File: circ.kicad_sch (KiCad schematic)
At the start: 2 parts

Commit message: Add files via upload
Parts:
- renumbered R22 to R30, U13 to U14
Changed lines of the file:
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@@
   (symbol (lib_id "Parts:J100N50X4B") (at 203.2 154.94 0) (unit 1)
     (in_bom yes) (on_board yes) (dnp no) (fields_autoplaced)
-    (property "Reference" "R22" (at 207.645 154.94 0)
+    (property "Reference" "R30" (at 207.645 154.94 0)
       (effects (font (size 1.27 1.27)) (justify left))
     )
@@
       (project "m17-rru-rf"
         (path "/4c42207c-9e6b-42da-ad38-da126b892014/52ad0992-68c2-4318-a1ac-e7f0506bc4fb"
-          (reference "R22") (unit 1)
+          (reference "R30") (unit 1)
         )
       )
@@
   (symbol (lib_id "Parts:WH3538X-1") (at 203.2 127 0) (unit 1)
     (in_bom yes) (on_board yes) (dnp no) (fields_autoplaced)
-    (property "Reference" "U13" (at 203.0795 115.4879 0)
+    (property "Reference" "U14" (at 203.0795 115.4879 0)
       (effects (font (size 1.27 1.27)))
     )
@@
       (project "m17-rru-rf"
         (path "/4c42207c-9e6b-42da-ad38-da126b892014/52ad0992-68c2-4318-a1ac-e7f0506bc4fb"
-          (reference "U13") (unit 1)
+          (reference "U14") (unit 1)
         )
       )

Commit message: Add files via upload
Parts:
- renumbered R30 to R34
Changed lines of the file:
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@@
   (symbol (lib_id "Parts:J100N50X4B") (at 203.2 154.94 0) (unit 1)
     (in_bom yes) (on_board yes) (dnp no) (fields_autoplaced)
-    (property "Reference" "R30" (at 207.645 154.94 0)
+    (property "Reference" "R34" (at 207.645 154.94 0)
       (effects (font (size 1.27 1.27)) (justify left))
     )
@@
       (project "m17-rru-rf"
         (path "/4c42207c-9e6b-42da-ad38-da126b892014/52ad0992-68c2-4318-a1ac-e7f0506bc4fb"
-          (reference "R30") (unit 1)
+          (reference "R34") (unit 1)
         )
       )

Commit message: Add files via upload
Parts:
- renumbered R34 to R37
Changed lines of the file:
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@@
   (symbol (lib_id "Parts:J100N50X4B") (at 203.2 154.94 0) (unit 1)
     (in_bom yes) (on_board yes) (dnp no) (fields_autoplaced)
-    (property "Reference" "R34" (at 207.645 154.94 0)
+    (property "Reference" "R37" (at 207.645 154.94 0)
       (effects (font (size 1.27 1.27)) (justify left))
     )
@@
       (project "m17-rru-rf"
         (path "/4c42207c-9e6b-42da-ad38-da126b892014/52ad0992-68c2-4318-a1ac-e7f0506bc4fb"
-          (reference "R34") (unit 1)
+          (reference "R37") (unit 1)
         )
       )

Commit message: Add files via upload
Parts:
- renumbered R37 to R40
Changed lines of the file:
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@@
   (symbol (lib_id "Parts:J100N50X4B") (at 203.2 154.94 0) (unit 1)
     (in_bom yes) (on_board yes) (dnp no) (fields_autoplaced)
-    (property "Reference" "R37" (at 207.645 154.94 0)
+    (property "Reference" "R40" (at 207.645 154.94 0)
       (effects (font (size 1.27 1.27)) (justify left))
     )
@@
       (project "m17-rru-rf"
         (path "/4c42207c-9e6b-42da-ad38-da126b892014/52ad0992-68c2-4318-a1ac-e7f0506bc4fb"
-          (reference "R37") (unit 1)
+          (reference "R40") (unit 1)
         )
       )

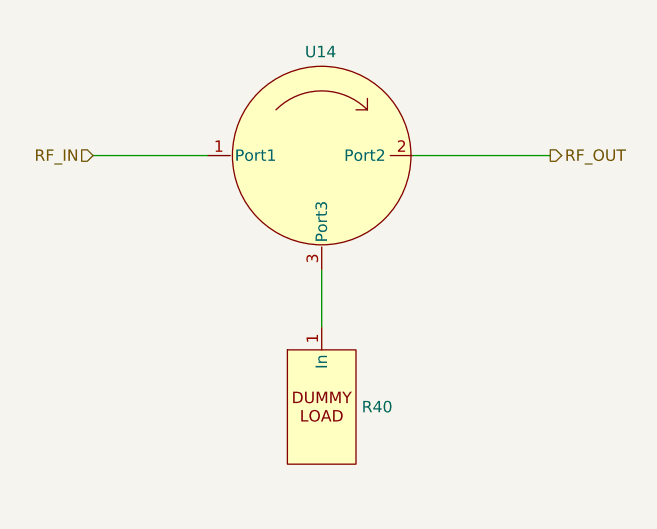
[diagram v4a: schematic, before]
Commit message: significant updates
- supply for the detector block changed from 3.3V to 5V
- minor bugfixes
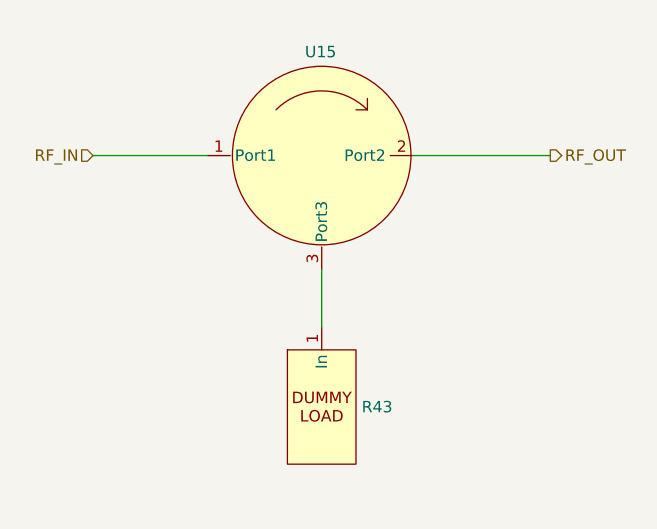
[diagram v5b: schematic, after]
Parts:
- renumbered R40 to R43, U14 to U15
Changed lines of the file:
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@@
   (symbol (lib_id "Parts:J100N50X4B") (at 203.2 154.94 0) (unit 1)
     (in_bom yes) (on_board yes) (dnp no) (fields_autoplaced)
-    (property "Reference" "R40" (at 207.645 154.94 0)
+    (property "Reference" "R43" (at 207.645 154.94 0)
       (effects (font (size 1.27 1.27)) (justify left))
     )
@@
       (project "m17-rru-rf"
         (path "/4c42207c-9e6b-42da-ad38-da126b892014/52ad0992-68c2-4318-a1ac-e7f0506bc4fb"
-          (reference "R40") (unit 1)
+          (reference "R43") (unit 1)
         )
       )
@@
   (symbol (lib_id "Parts:WH3538X-1") (at 203.2 127 0) (unit 1)
     (in_bom yes) (on_board yes) (dnp no) (fields_autoplaced)
-    (property "Reference" "U14" (at 203.0795 115.4879 0)
+    (property "Reference" "U15" (at 203.0795 115.4879 0)
       (effects (font (size 1.27 1.27)))
     )
@@
       (project "m17-rru-rf"
         (path "/4c42207c-9e6b-42da-ad38-da126b892014/52ad0992-68c2-4318-a1ac-e7f0506bc4fb"
-          (reference "U14") (unit 1)
+          (reference "U15") (unit 1)
         )
       )

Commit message: PN update
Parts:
- R43: value ~ -> J100N50X4B
- U15: value ~ -> WH3538X-1
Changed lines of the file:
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@@
       (effects (font (size 1.27 1.27)) (justify left))
     )
-    (property "Value" "~" (at 203.2 148.59 0)
+    (property "Value" "J100N50X4B" (at 203.2 148.59 0)
       (effects (font (size 1.27 1.27)))
     )
@@
       (effects (font (size 1.27 1.27)))
     )
-    (property "Value" "~" (at 203.2 113.03 0)
+    (property "Value" "WH3538X-1" (at 203.2 113.03 0)
       (effects (font (size 1.27 1.27)))
     )

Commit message: date and labels update
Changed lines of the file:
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@@
   (title_block
     (title "M17 Remote Radio Unit - RF board")
-    (date "10-10-2023")
+    (date "15-10-2023")
     (rev "A")
     (company "M17 Project")
@@
   )
   (symbol (lib_id "Parts:J100N50X4B") (at 203.2 154.94 0) (unit 1)
-    (in_bom yes) (on_board yes) (dnp no) (fields_autoplaced)
-    (property "Reference" "R43" (at 207.645 154.94 0)
-      (effects (font (size 1.27 1.27)) (justify left))
-    )
-    (property "Value" "J100N50X4B" (at 203.2 148.59 0)
+    (in_bom yes) (on_board yes) (dnp no)
+    (property "Reference" "R43" (at 203.2 162.56 0)
       (effects (font (size 1.27 1.27)))
     )
+    (property "Value" "J100N50X4B" (at 203.2 165.1 0)
+      (effects (font (size 1.27 1.27)))
+    )

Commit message: pcb update
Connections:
- net ISOLATED: now reaches R43.1 (In), U15.3 (Port3)
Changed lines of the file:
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@@
   (title_block
     (title "M17 Remote Radio Unit - RF board")
-    (date "15-10-2023")
+    (date "27-10-2023")
     (rev "A")
     (company "M17 Project")
@@
     (stroke (width 0) (type default))
   )
+  (label "ISOLATED" (at 203.2 143.51 0) (fields_autoplaced)
+    (effects (font (size 1.27 1.27)) (justify left bottom))
+  )
   (hierarchical_label "RF_OUT" (shape output) (at 228.6 127 0) (fields_autoplaced)
